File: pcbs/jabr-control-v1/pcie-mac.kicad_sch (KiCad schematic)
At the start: 1 part, among them U5001 LAN7431_YXX

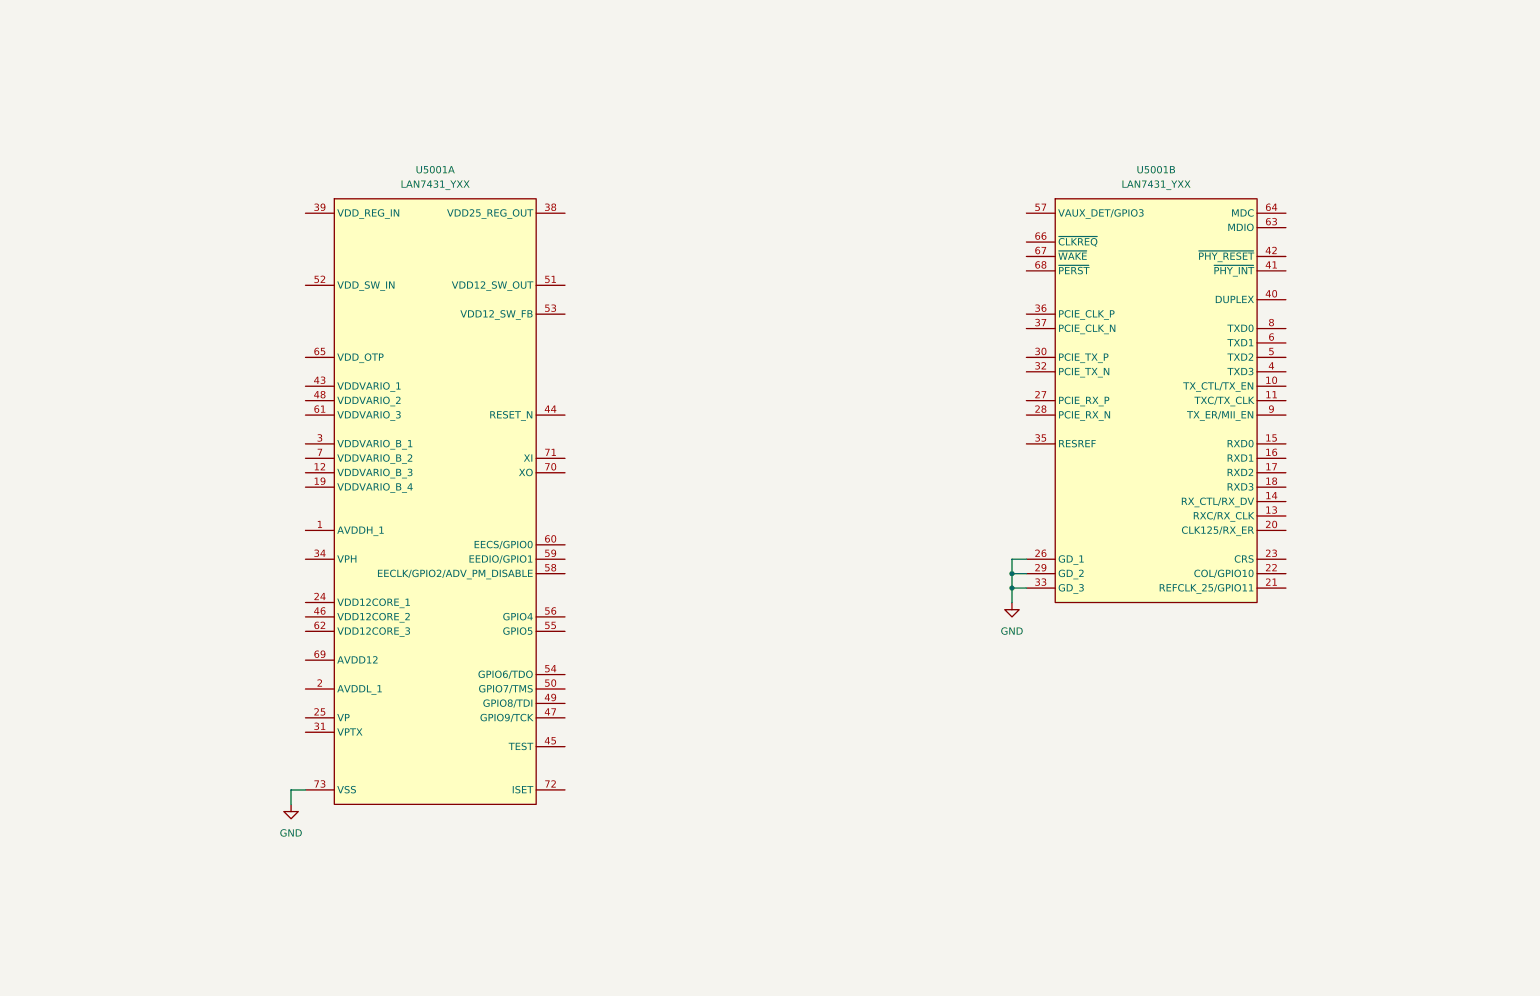
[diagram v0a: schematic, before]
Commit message: Added PCIe connections
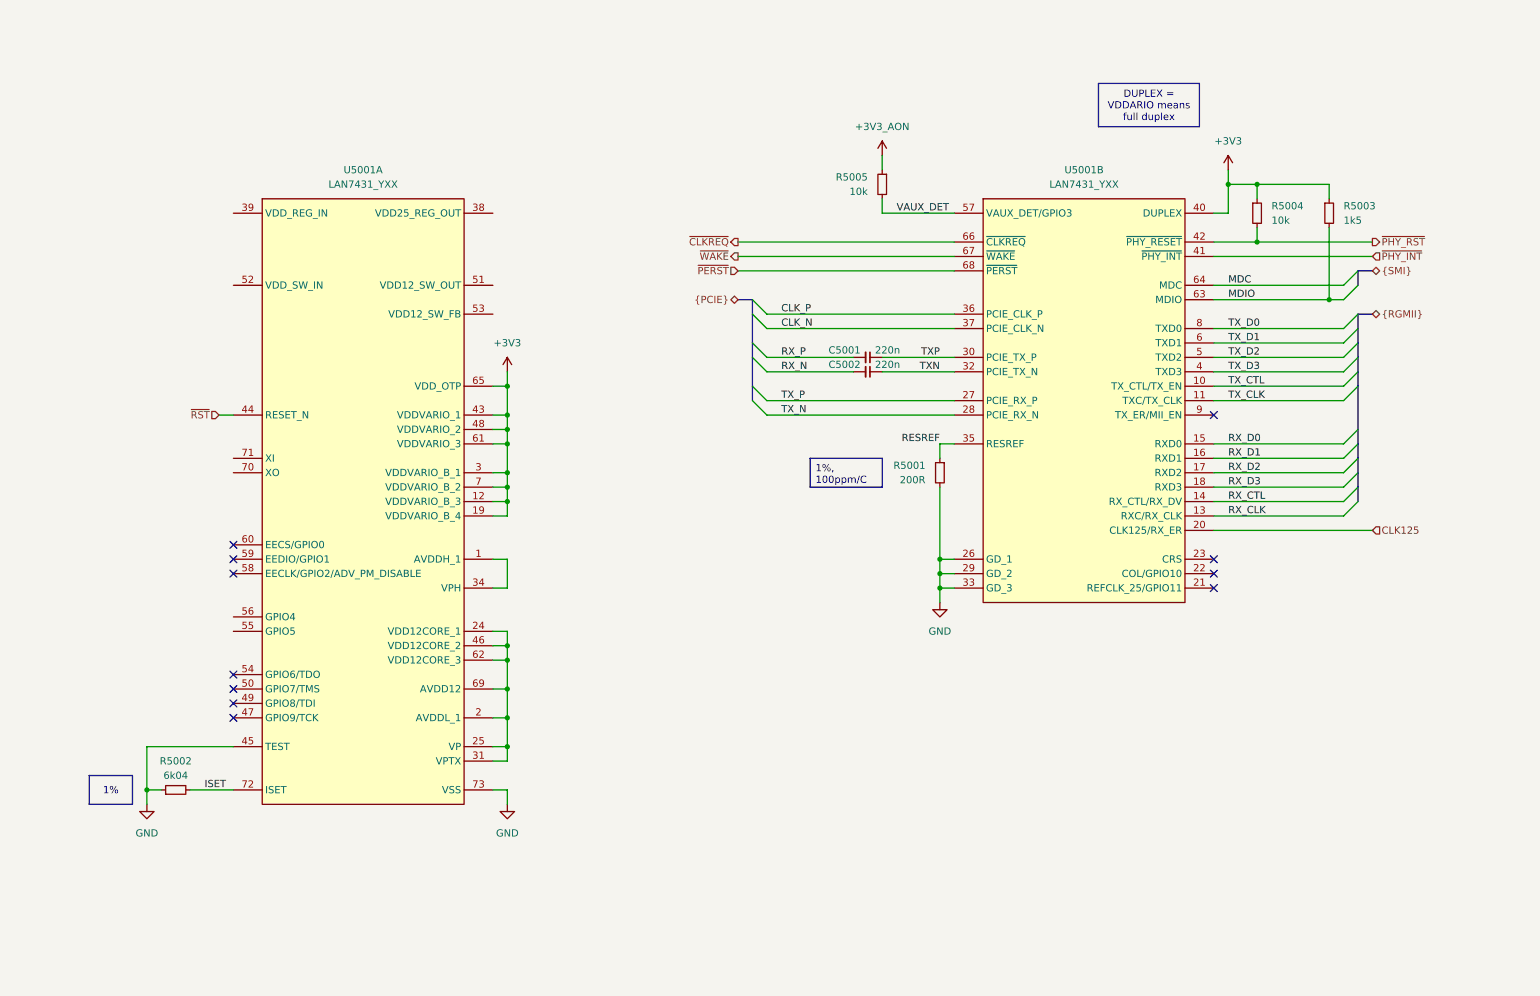
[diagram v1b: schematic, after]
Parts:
- added C5001, C5002: 220n, project_footprints:C_0402, symbol DEV:C_TINY_IO
- added R5001: 200R, project_footprints:R_0402, symbol DEV:R_SMALL
- added R5002: 6k04, symbol DEV:R_SMALL
- added R5003: 1k5, project_footprints:R_0402, symbol DEV:R_SMALL
- added R5004, R5005: 10k, project_footprints:R_0402, symbol DEV:R_SMALL
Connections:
- net GND: now also U5001.45 (TEST), R5001.2, R5002.1
- net TX_CTL: now reaches U5001.10 (TX_CTL/TX_EN)
- net TX_CLK: now reaches U5001.11 (TXC/TX_CLK)
- net RX_CLK: now reaches U5001.13 (RXC/RX_CLK)
- net RX_CTL: now reaches U5001.14 (RX_CTL/RX_DV)
- net RX_D0: now reaches U5001.15 (RXD0)
- net RX_D1: now reaches U5001.16 (RXD1)
- net RX_D2: now reaches U5001.17 (RXD2)
- net RX_D3: now reaches U5001.18 (RXD3)
- net CLK125: now reaches U5001.20 (CLK125/RX_ER)
- net TX_P: now reaches U5001.27 (PCIE_RX_P)
- net TX_N: now reaches U5001.28 (PCIE_RX_N)
- net TXP: now reaches U5001.30 (PCIE_TX_P)
- net TXP: now also C5001.1
- net TXN: now reaches U5001.32 (PCIE_TX_N)
- net TXN: now also C5002.1
- net RESREF: now reaches U5001.35 (RESREF)
- net RESREF: now also R5001.1
- net CLK_P: now reaches U5001.36 (PCIE_CLK_P)
- net CLK_N: now reaches U5001.37 (PCIE_CLK_N)
- net TX_D3: now reaches U5001.4 (TXD3)
- net +3V3: now reaches U5001.40 (DUPLEX)
- net +3V3: now also U5001.12 (VDDVARIO_B_3), U5001.19 (VDDVARIO_B_4), U5001.3 (VDDVARIO_B_1), U5001.43 (VDDVARIO_1), U5001.48 (VDDVARIO_2), U5001.61 (VDDVARIO_3), U5001.65 (VDD_OTP), U5001.7 (VDDVARIO_B_2), R5003.1, R5004.1
- net ~{PHY_INT}: now reaches U5001.41 (~{PHY_INT})
- net ~{PHY_RST}: now reaches U5001.42 (~{PHY_RESET})
- net ~{PHY_RST}: now also R5004.2
- net TX_D2: now reaches U5001.5 (TXD2)
- net VAUX_DET: now reaches U5001.57 (VAUX_DET/GPIO3)
- net VAUX_DET: now also R5005.2
- net TX_D1: now reaches U5001.6 (TXD1)
- net MDIO: now reaches U5001.63 (MDIO)
- net MDIO: now also R5003.2
- net MDC: now reaches U5001.64 (MDC)
- net ~{CLKREQ}: now reaches U5001.66 (~{CLKREQ})
- net ~{WAKE}: now reaches U5001.67 (~{WAKE})
- net ~{PERST}: now reaches U5001.68 (~{PERST})
- net TX_D0: now reaches U5001.8 (TXD0)
- net at U5001.1 (AVDDH_1): now also U5001.34 (VPH)
- net at U5001.2 (AVDDL_1): now also U5001.24 (VDD12CORE_1), U5001.25 (VP), U5001.31 (VPTX), U5001.46 (VDD12CORE_2), U5001.62 (VDD12CORE_3), U5001.69 (AVDD12)
- net ~{RST}: now reaches U5001.44 (RESET_N)
- net ISET: now reaches U5001.72 (ISET)
- net ISET: now also R5002.2
- new net +3V3_AON: R5005.1
- new net RX_N: C5002.2
- new net RX_P: C5001.2
- no-connect marks 0 -> 11
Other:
- moved on the sheet: U5001A, U5001B

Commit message: Worked on power and other areas of the schematic
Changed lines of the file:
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@@
 	(text_box "DUPLEX = VDDARIO means full duplex"
 		(exclude_from_sim no)
-		(at 205.74 30.48 0)
-		(size 17.78 7.62)
+		(at 236.22 38.1 0)
+		(size 22.86 5.08)
 		(margins 0.9525 0.9525 0.9525 0.9525)
 		(stroke
@@
 				(size 1.27 1.27)
 			)
+			(justify left)
 		)
 	)
@@
 				(size 1.27 1.27)
 			)
-			(justify left top)
+			(justify left)
 		)
 	)

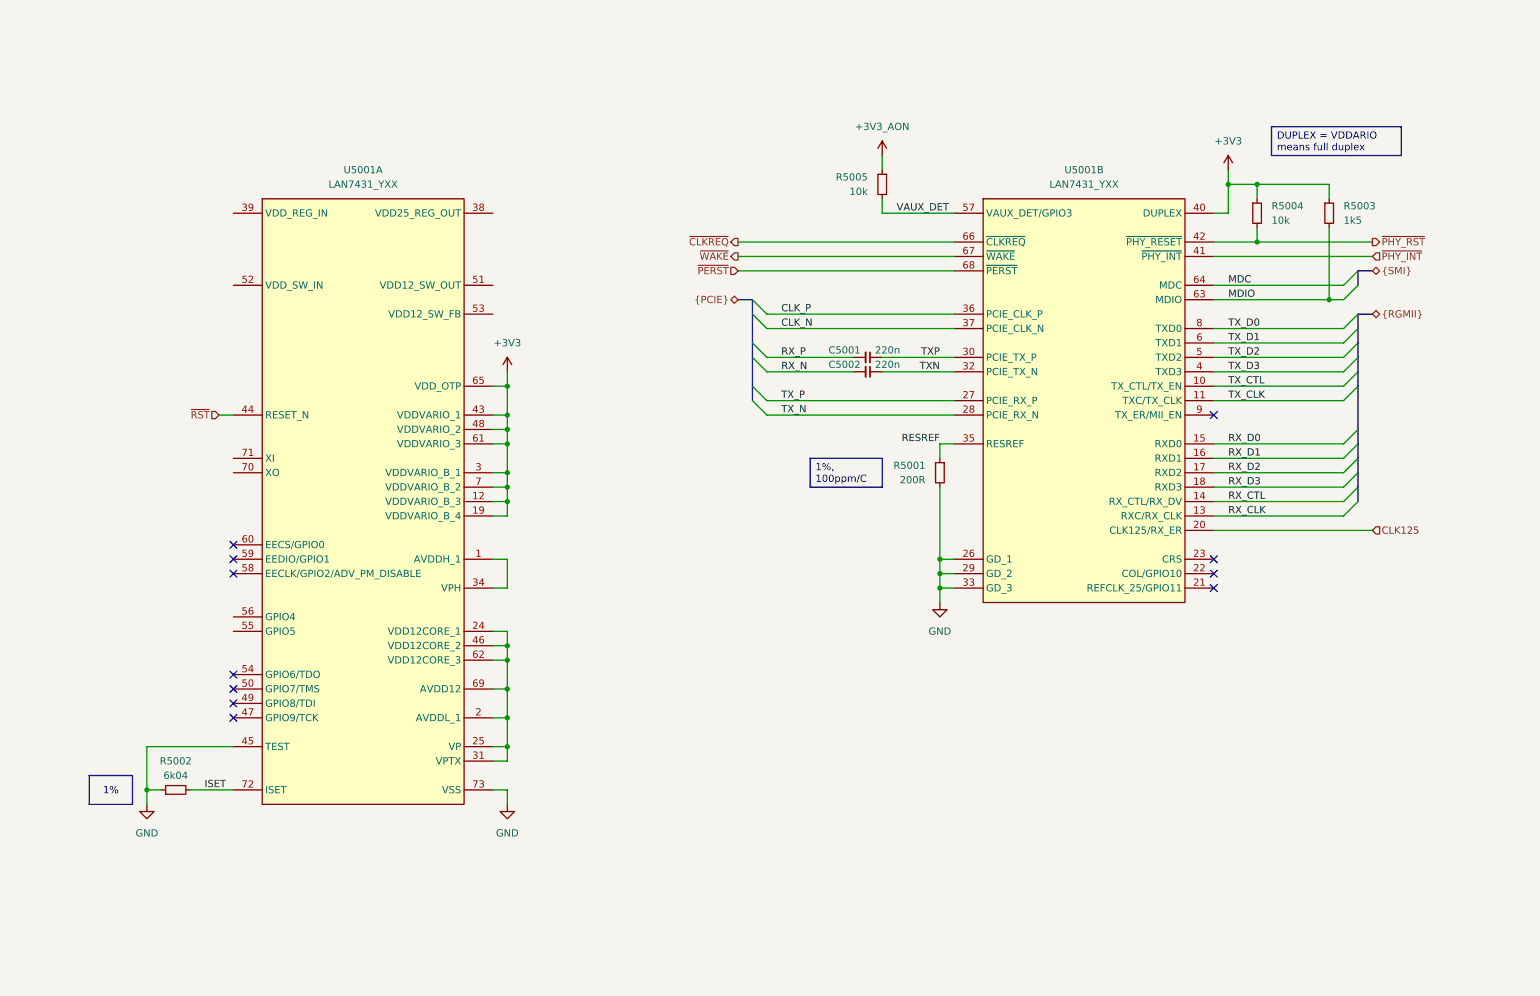
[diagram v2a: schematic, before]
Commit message: Progress on LAN7431 power
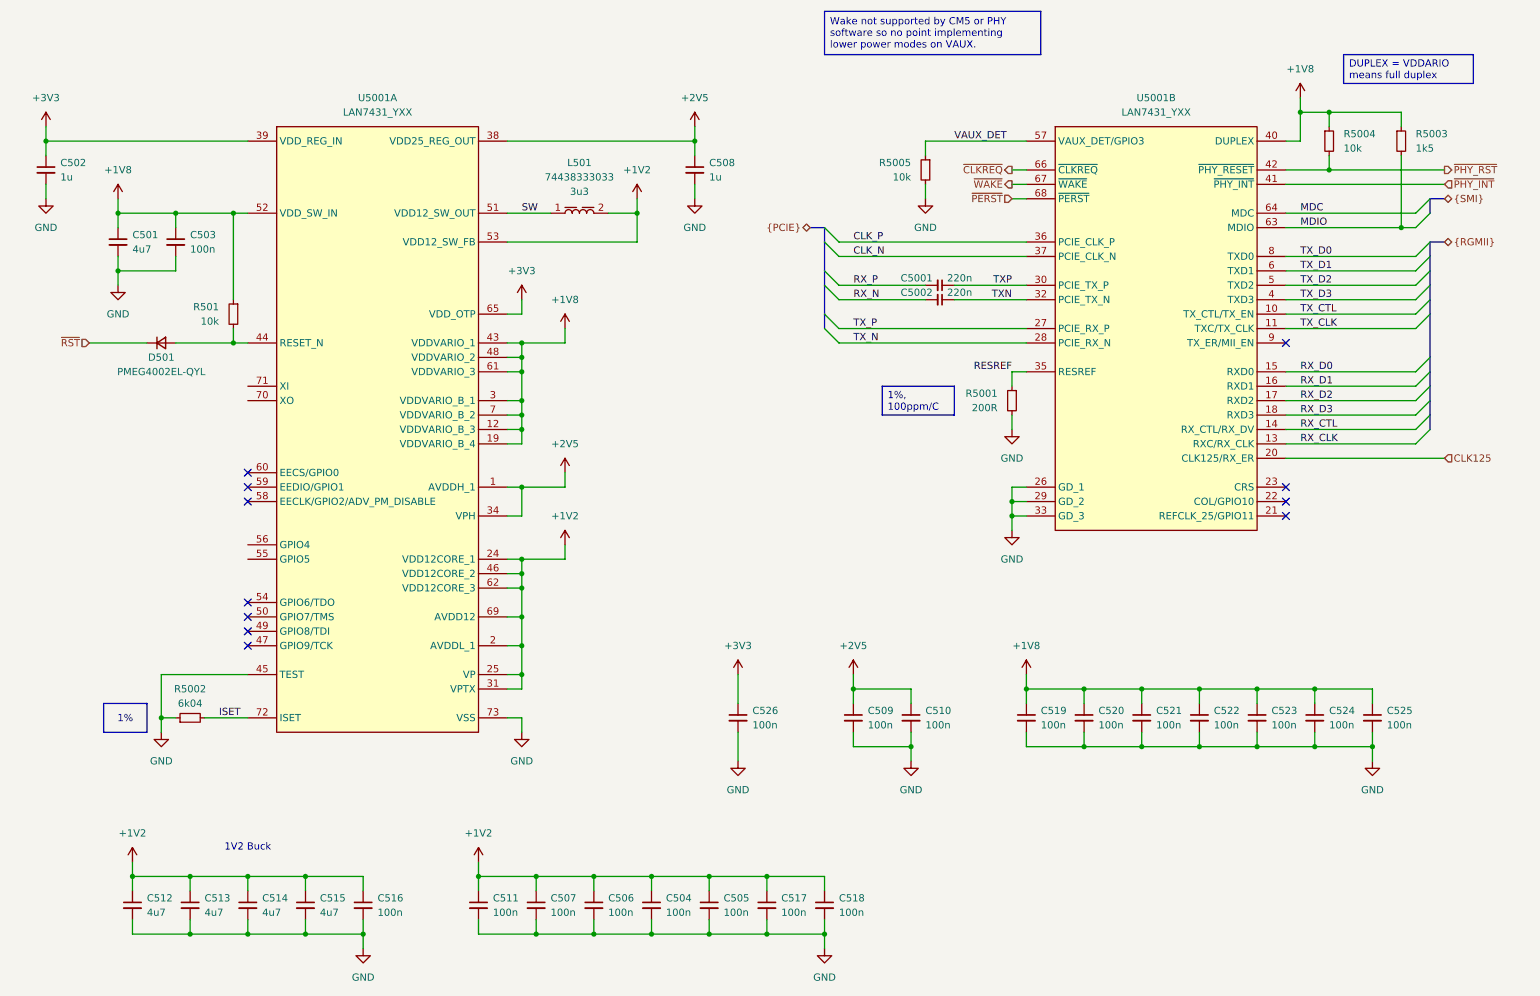
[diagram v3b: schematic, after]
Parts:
- added C501, C512, C513, C514, C515: 4u7, project_footprints:C_0402, symbol DEV:C_SMALL_IO
- added C502, C508: 1u, project_footprints:C_0402, symbol DEV:C_SMALL_IO
- added C503, C504, C505, C506, C507, C509, C510, C511, C516, C517, C518, C519, C520, C521, C522, C523, C524, C525, C526: 100n, project_footprints:C_0402, symbol DEV:C_SMALL_IO
- added D501: PMEG4002EL-QYL, project_footprints:PMEG4002EL-QYL, symbol DIODE:PMEG4002EL-QYL
- added L501: 74438333033, project_footprints:L_Wurth_WE-MAPI-3010, symbol PWR-IND:3010_74438333033
- added R501: 10k, project_footprints:R_0402, symbol DEV:R_SMALL
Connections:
- net +3V3_AON is gone; now on net VAUX_DET: R5005.1
- net +3V3: now also U5001.39 (VDD_REG_IN), C502.1, C526.1; no longer R5003.1, R5004.1, U5001.12 (VDDVARIO_B_3), U5001.19 (VDDVARIO_B_4), U5001.3 (VDDVARIO_B_1), U5001.40 (DUPLEX), U5001.43 (VDDVARIO_1), U5001.48 (VDDVARIO_2), U5001.61 (VDDVARIO_3), U5001.7 (VDDVARIO_B_2)
- net GND: now also R5005.2, C501.2, C502.2, C503.2, C504.2, C505.2, C506.2, C507.2, C508.2, C509.2, C510.2, C511.2, C512.2, C513.2, C514.2, C515.2, C516.2, C517.2, C518.2, C519.2, C520.2, C521.2, C522.2, C523.2, C524.2, C525.2, C526.2
- net VAUX_DET: no longer R5005.2
- net ~{RST}: now also D501.1 (K); no longer U5001.44 (RESET_N)
- net +2V5: now reaches U5001.1 (AVDDH_1), U5001.34 (VPH)
- net +2V5: now also U5001.38 (VDD25_REG_OUT), C508.1, C509.1, C510.1
- net +1V2: now reaches U5001.2 (AVDDL_1), U5001.24 (VDD12CORE_1), U5001.25 (VP), U5001.31 (VPTX), U5001.46 (VDD12CORE_2), U5001.62 (VDD12CORE_3), U5001.69 (AVDD12)
- net +1V2: now also U5001.53 (VDD12_SW_FB), C504.1, C505.1, C506.1, C507.1, C511.1, C512.1, C513.1, C514.1, C515.1, C516.1, C517.1, C518.1, L501.2
- net SW: now reaches U5001.51 (VDD12_SW_OUT)
- net SW: now also L501.1
- net +1V8: now reaches U5001.52 (VDD_SW_IN)
- net +1V8: now also R5003.1, R5004.1, U5001.12 (VDDVARIO_B_3), U5001.19 (VDDVARIO_B_4), U5001.3 (VDDVARIO_B_1), U5001.40 (DUPLEX), U5001.43 (VDDVARIO_1), U5001.48 (VDDVARIO_2), U5001.61 (VDDVARIO_3), U5001.7 (VDDVARIO_B_2), C501.1, C503.1, C519.1, C520.1, C521.1, C522.1, C523.1, C524.1, C525.1, R501.1
- new net: D501.2 (A), R501.2, U5001.44 (RESET_N)
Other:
- note added: "1V2 Buck"
- moved on the sheet: C5001, C5002, R5001, R5002, R5003, R5004, R5005, U5001A, U5001B
